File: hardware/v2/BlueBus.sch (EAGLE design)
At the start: 142 parts, among them J1 3PIN_953442_1, J2 6PIN_953442_1, J3 6PIN_5_103166_1, J4 SJ2-35853A-SMT-TR, J5 SMB_CONN, J6 USB3080-30-01-A, J7 PCM12SMTR, J8 TC2030NL, Q1 NMOSFET-BSS138K, Q2 NMOSFET-BSS138K, Q3 PMOSFET-DMP32D4SSOT323, U1 MPQ4420, U10 PCM5122, U11 PAM8406, U2 TH3122.4, U3 FT231XS, U4 S-1212BC0-U5T1U, U5 XC6210, U6 CAT25M01, U7 PIC24FJ1024GA606, U8 BM83SM1, U9 DIT4096

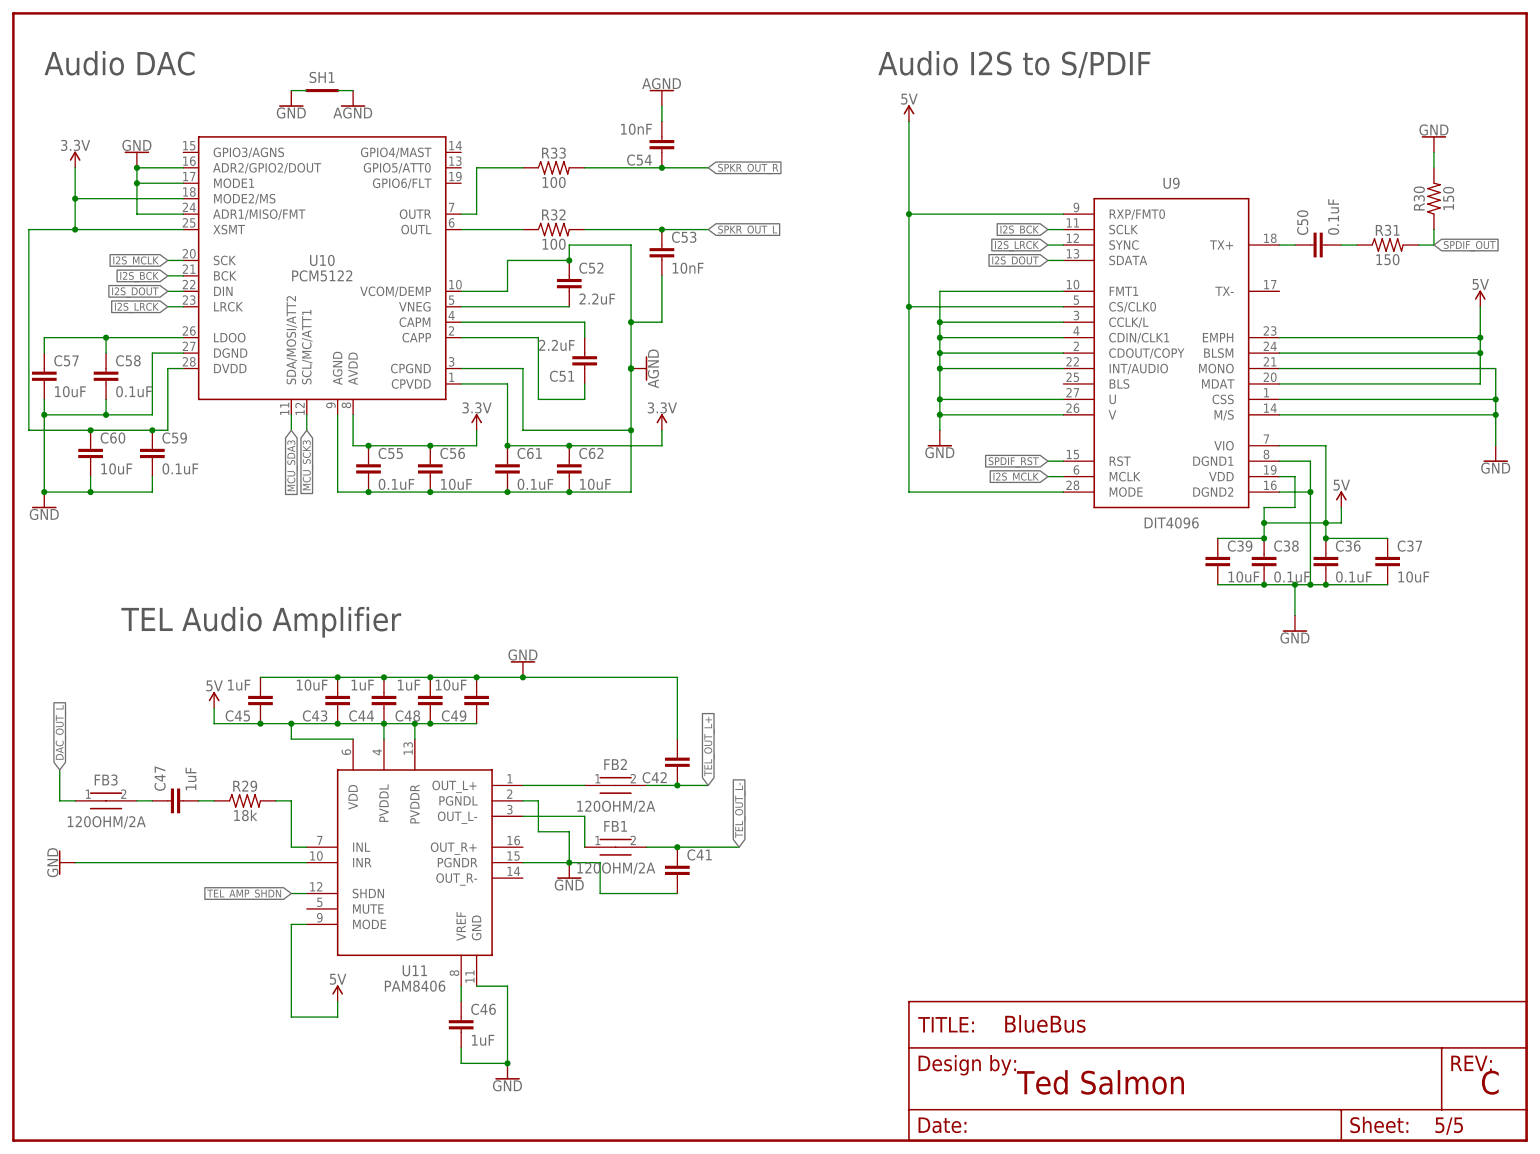
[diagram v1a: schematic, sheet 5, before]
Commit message: [IMP] hardware: v2 Bugfixes * Ensure 100nF caps are closest to pins instead of 10uF/1uF * Fix bottom silkscreen * Fix recovery slider silkscreen * Renumber passives per convention (counter-clockwise)
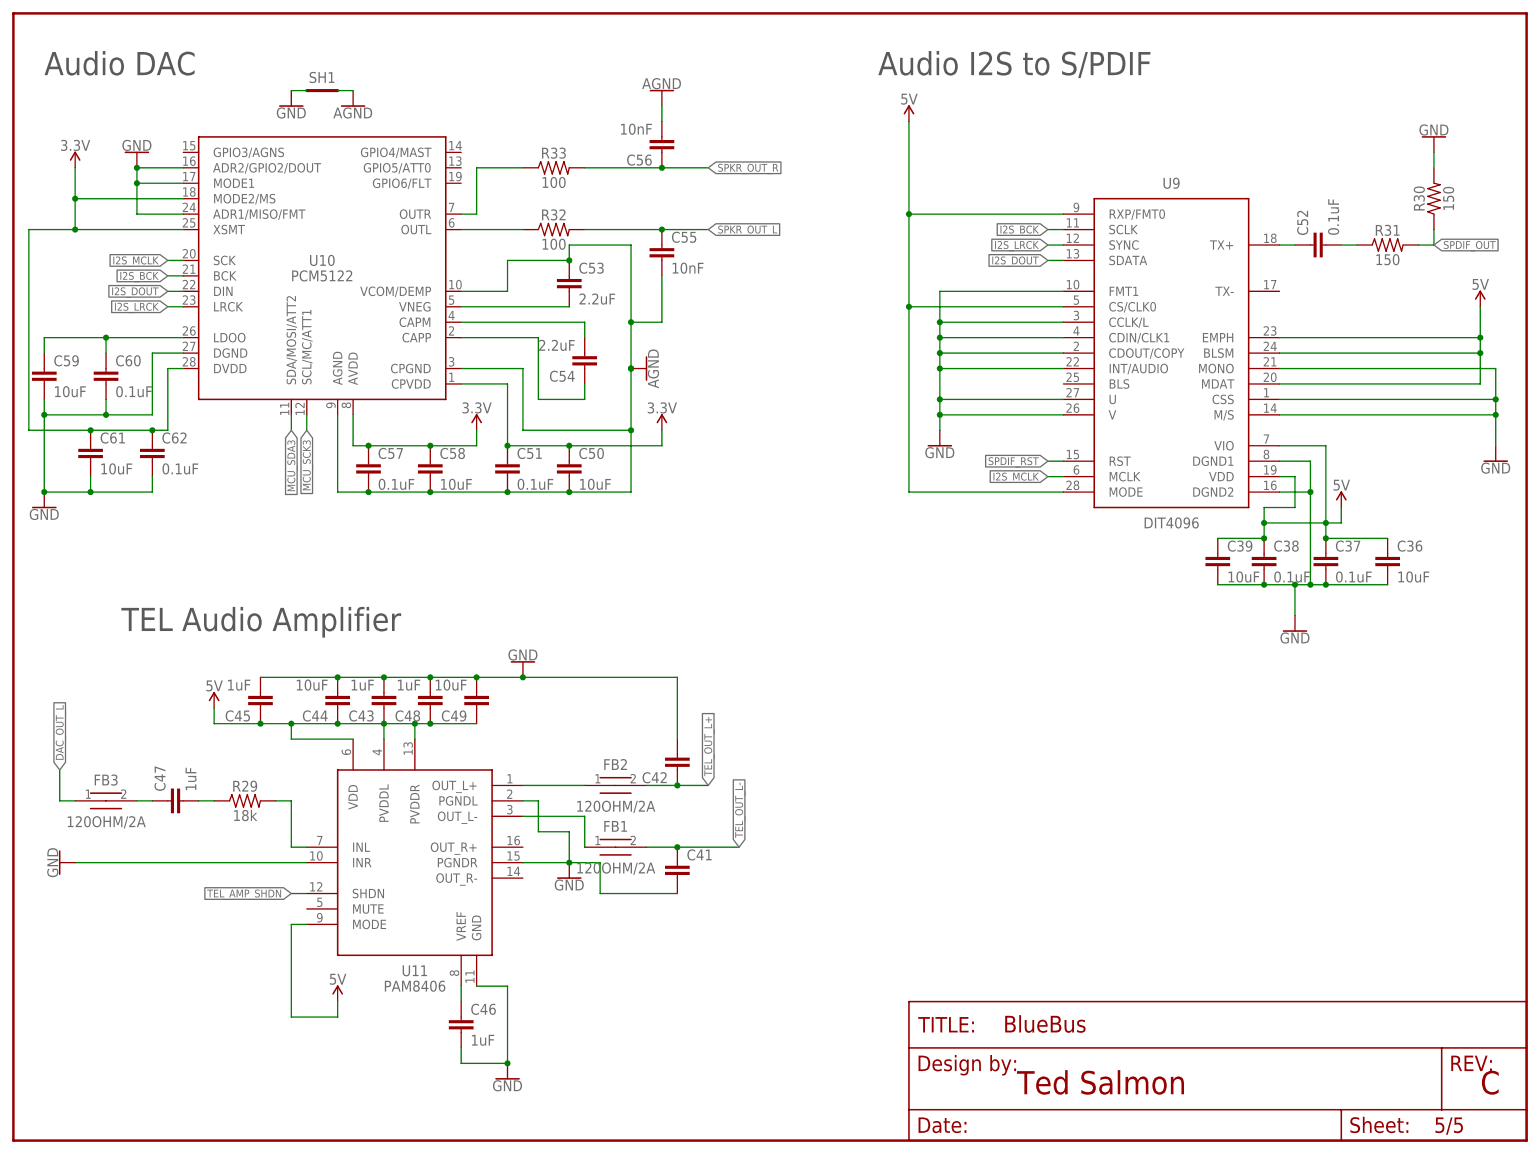
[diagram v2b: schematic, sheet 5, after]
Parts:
- C24, C36, C50, C58, C59, C61: value 0.1uF -> 10uF; device Passives:0.1UF0603 -> Passives:10UF0603
- C26, C37, C57, C60, C62: value 10uF -> 0.1uF; device Passives:10UF0603 -> Passives:0.1UF0603
- C43: value 10uF -> 1uF; device Passives:10UF0603 -> Passives:1UF0603
- C44: value 1uF -> 10uF; device Passives:1UF0603 -> Passives:10UF0603
- C51, C52: value 2.2uF -> 0.1uF; device Passives:2.2UF0603 -> Passives:0.1UF0603
- C53, C54: value 10nF -> 2.2uF; device Passives:10NF0603 -> Passives:2.2UF0603
- C55: value 0.1uF -> 10nF; device Passives:0.1UF0603 -> Passives:10NF0603
- C56: value 10uF -> 10nF; device Passives:10UF0603 -> Passives:10NF0603
- R8: value 20 -> 100k; device Passives:20OHM0603 -> Passives:100KOHM0603
- R9: value 100k -> 20; device Passives:100KOHM0603 -> Passives:20OHM0603
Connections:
- net 3.3V: now also C50.1, C51.1, C57.1, C58.1; no longer C55.1, C56.1, C59.1, C60.1
- net 5V: now also C24.1; no longer C26.1
- net 5VREG_BS: now also R9.1; no longer R8.1
- net 5VREG_BS_CAP: now also C7.1, R9.2; no longer C11.1, R8.2
- net 5VREG_EN: now also R8.1; no longer R9.1
- net 5VREG_SW: now also C7.2; no longer C11.2
- net 5VREG_VCC: now also C8.1; no longer C7.1
- net AGND: now also C50.2, C51.2, C53.1, C57.2, C58.2; no longer C52.1, C53.2, C54.2, C61.2, C62.2
- net DAC_CAPM: now also C54.2; no longer C51.2
- net DAC_CAPP: now also C54.1; no longer C51.1
- net DAC_LDOO: now also C59.1, C60.1; no longer C57.1, C58.1
- net DAC_VNEG: now also C53.2; no longer C52.2
- net GND: now also C11.2, C61.2, C62.2; no longer C57.2, C58.2, C7.2
- net IBUS_5V: now also R8.2; no longer R9.2
- net SPDIF_TX_FLT: now also C52.1; no longer C50.1
- net SPDIF_TX_RES: now also C52.2; no longer C50.2
- net SPKR_OUT_L: now also C55.1; no longer C53.1
- net SPKR_OUT_R: now also C56.1; no longer C54.1
- net USB_3V3: now also C26.1; no longer C24.1
- net VIN: now also C11.1; no longer C8.1
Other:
- moved on the sheet: C10, C11, C24, C26, C36, C37, C43, C44, C50, C51, C52, C53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

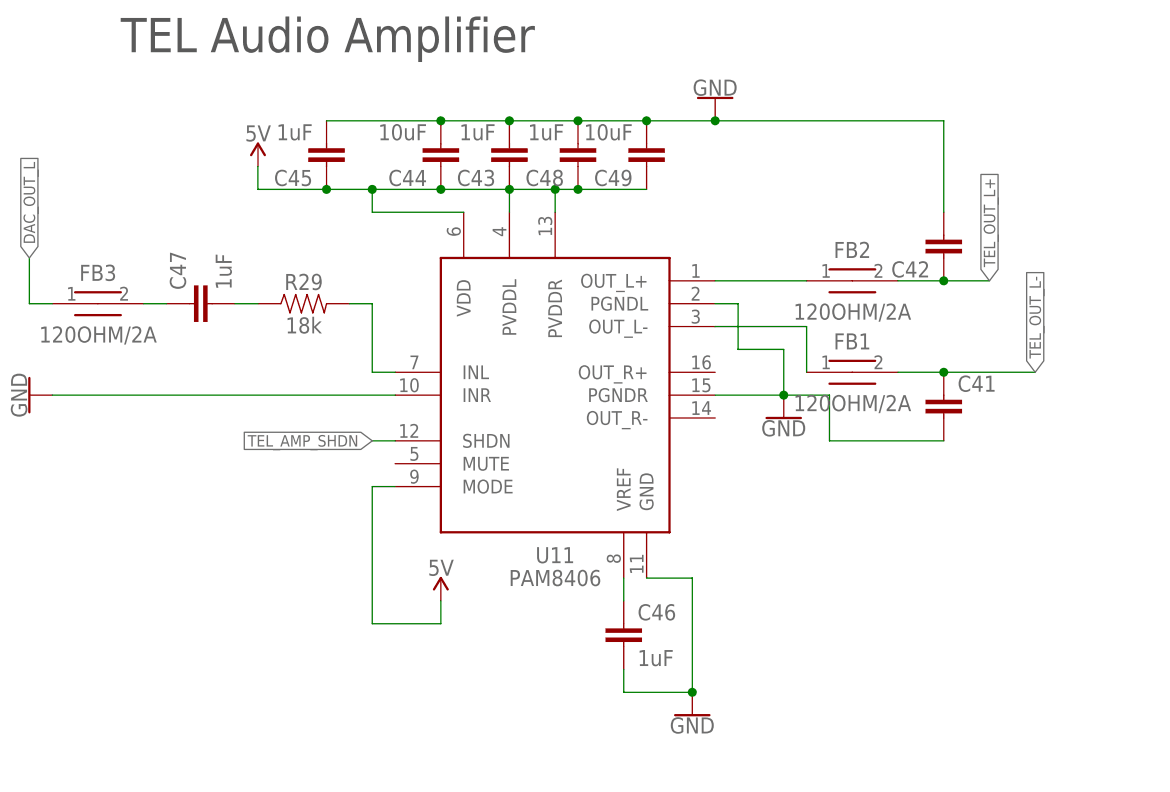
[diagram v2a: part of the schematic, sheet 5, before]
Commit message: [IMP] hardware: v2 Bugfixes * Re-number capacitors per convention and ensure proper placement
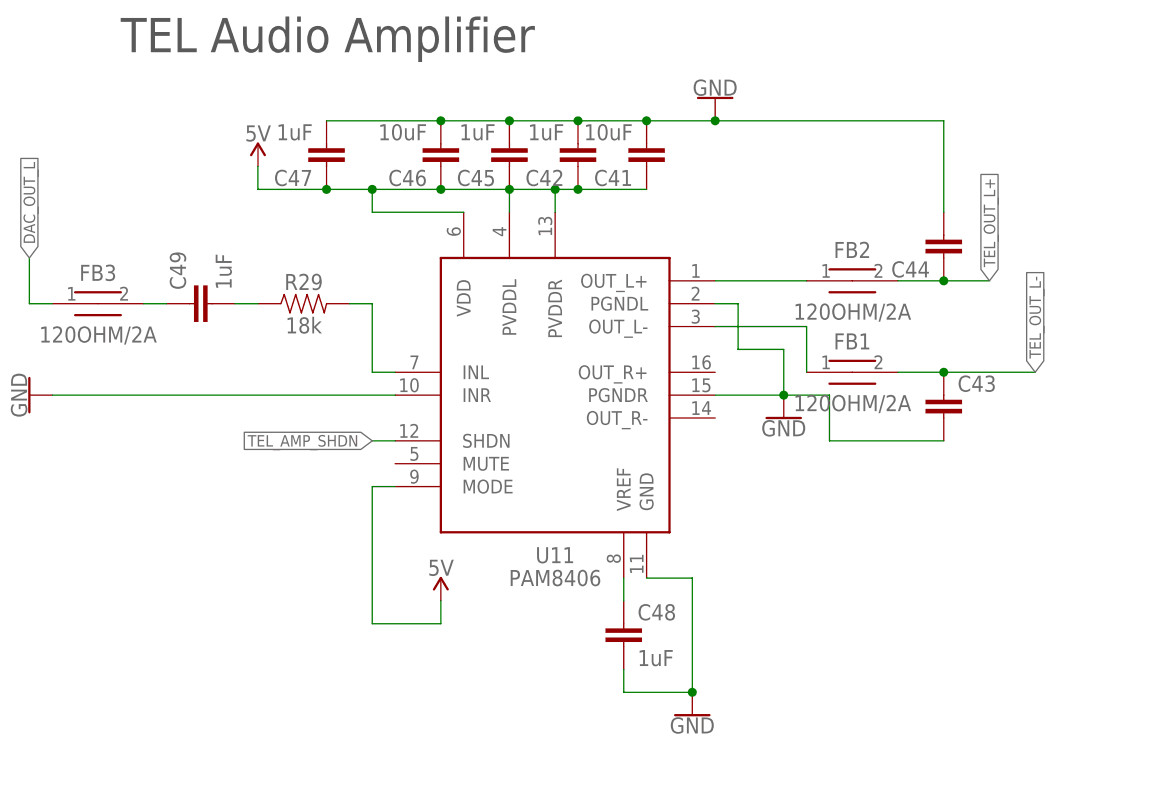
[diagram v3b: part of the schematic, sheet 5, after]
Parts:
- C1: value RHS1V101MCN1GS -> 0.1uF; device Passives:RHS1V101MCN1GS -> Passives:0.1UF0603
- C18: value 10uF -> 0.1uF; device Passives:10UF0603 -> Passives:0.1UF0603
- C19: value 0.1uF -> 10uF; device Passives:0.1UF0603 -> Passives:10UF0603
- C2: value 0.1uF -> 2.2uF; device Passives:0.1UF0603 -> Passives:2.2UF0603
- C3: value 2.2uF -> 1uF; device Passives:2.2UF0603 -> Passives:1UF0603
- C31: value 1uF -> 47nF; device Passives:1UF0603 -> Passives:47NF0603
- C32, C43: value 1uF -> 200pF; device Passives:1UF0603 -> Passives:220PF0603
- C34, C42: value 200pF -> 1uF; device Passives:220PF0603 -> Passives:1UF0603
- C35: value 47nF -> 1uF; device Passives:47NF0603 -> Passives:1UF0603
- C4: value 1uF -> RHS1V101MCN1GS; device Passives:1UF0603 -> Passives:RHS1V101MCN1GS
- C41: value 200pF -> 10uF; device Passives:220PF0603 -> Passives:10UF0603
- C44: value 10uF -> 200pF; device Passives:10UF0603 -> Passives:220PF0603
- C46: value 1uF -> 10uF; device Passives:1UF0603 -> Passives:10UF0603
- C49: value 10uF -> 1uF; device Passives:10UF0603 -> Passives:1UF0603
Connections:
- net 12V: now also C2.1; no longer C3.1
- net 3.3V: now also C1.1, C17.2; no longer C2.1, C20.2
- net 5V: now also C41.1, C42.1, C46.1, C47.1; no longer C43.1, C44.1, C48.1, C49.1
- net BT_MIC_L: now also C32.1, R27.1; no longer C34.1, R26.1
- net GND: now also C17.1, C20.2, C31.1, C35.2, C47.2; no longer C17.2, C20.1, C31.2, C35.1, C49.2
- net MCU_MCLR_RES: now also C20.1; no longer C19.1
- net MCU_VCAP: now also C19.1; no longer C17.1
- net MICN1: now also C31.2; no longer C35.2
- net MICP1_RES: now also C35.1, R26.1, R27.2; no longer C31.1, R26.2, R27.1
- net MIC_BIAS: now also C34.1, R26.2; no longer C32.1, R27.2
- net TEL_AMP_IN: now also C49.1; no longer C47.1
- net TEL_AMP_INL_CAP_RES: now also C49.2; no longer C47.2
- net TEL_AMP_VREF: now also C48.1; no longer C46.1
- net TEL_OUT_L+: now also C44.1; no longer C42.1
- net TEL_OUT_L-: now also C43.1; no longer C41.1
- net VIN: now also C3.1; no longer C1.1
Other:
- moved on the sheet: C14, C15, C16, C17, C18, C19, C2, C20, C3, C31, C32, C34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

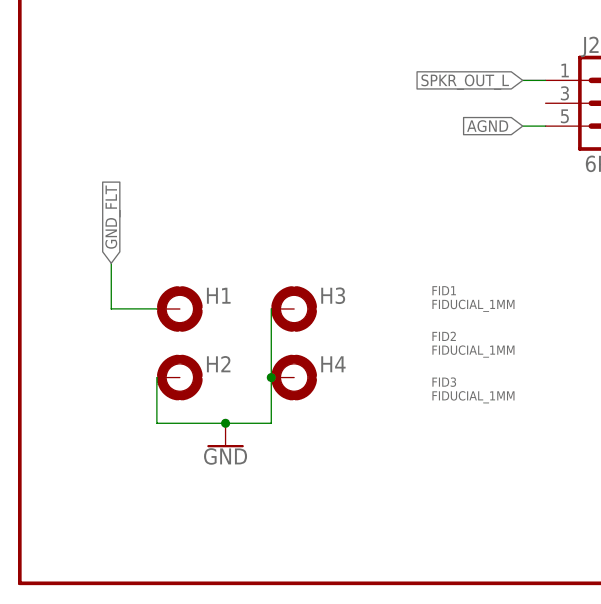
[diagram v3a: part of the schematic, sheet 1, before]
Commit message: [IMP] hardware: v2 Hardware updates for manufacture * Remove USB cutout * Swap PTH holes to simple holes * Add tCream to USB mount holes
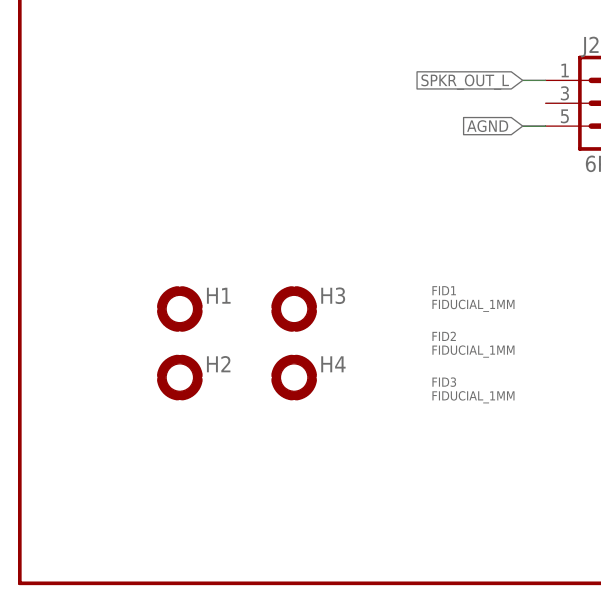
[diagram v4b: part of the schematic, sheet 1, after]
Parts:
- H1, H2, H3, H4: value 2,5-PAD -> 2,5-HOLE; device Connectors:2,5-PAD -> Connectors:2,5-HOLE
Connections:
- net GND: no longer H2.MOUNT, H3.MOUNT, H4.MOUNT
- net GND_FLT: no longer H1.MOUNT
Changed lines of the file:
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@@
 <part name="FRAME4" library="Frame" deviceset="FRAME-LETTER" device="" package3d_urn="urn:adsk.eagle:package:37104/1"/>
 <part name="U10" library="ICs" deviceset="PCM5122" device="" value="PCM5122"/>
-<part name="H1" library="Connectors" deviceset="2,5-PAD" device=""/>
-<part name="H2" library="Connectors" deviceset="2,5-PAD" device=""/>
-<part name="H3" library="Connectors" deviceset="2,5-PAD" device=""/>
-<part name="H4" library="Connectors" deviceset="2,5-PAD" device=""/>
-<part name="GND28" library="SparkFun-PowerSymbols" library_urn="urn:adsk.eagle:library:530" deviceset="GND" device=""/>
+<part name="H1" library="Connectors" deviceset="2,5-HOLE" device=""/>
+<part name="H2" library="Connectors" deviceset="2,5-HOLE" device=""/>
+<part name="H3" library="Connectors" deviceset="2,5-HOLE" device=""/>
+<part name="H4" library="Connectors" deviceset="2,5-HOLE" device=""/>
 <part name="FB3" library="Passives" deviceset="FERRITE_2A/120OHM" device="0603" value="120OHM/2A"/>
 <part name="F1" library="Passives" deviceset="LITTLEBLOCK_FUSE_.75A" device="" value="750mA"/>
@@
 <attribute name="NAME" x="33.274" y="23.4442" size="1.778" layer="95"/>
 </instance>
-<instance part="GND28" gate="1" x="22.86" y="15.24" smashed="yes">
-<attribute name="VALUE" x="22.86" y="14.986" size="1.778" layer="96" align="top-center"/>
-</instance>
 <instance part="F1" gate="G$1" x="182.88" y="157.48" smashed="yes">
 <attribute name="NAME" x="182.88" y="162.56" size="1.778" layer="95" font="vector" align="center"/>
@@
 </segment>
 <segment>
-<pinref part="H2" gate="G$1" pin="MOUNT"/>
-<pinref part="GND28" gate="1" pin="GND"/>
-<wire x1="15.24" y1="22.86" x2="15.24" y2="17.78" width="0.1524" layer="91"/>
-<wire x1="15.24" y1="17.78" x2="22.86" y2="17.78" width="0.1524" layer="91"/>
-<pinref part="H3" gate="G$1" pin="MOUNT"/>
-<pinref part="H4" gate="G$1" pin="MOUNT"/>
-<wire x1="27.94" y1="30.48" x2="27.94" y2="22.86" width="0.1524" layer="91"/>
-<wire x1="27.94" y1="22.86" x2="27.94" y2="17.78" width="0.1524" layer="91"/>
-<wire x1="27.94" y1="17.78" x2="22.86" y2="17.78" width="0.1524" layer="91"/>
-<junction x="27.94" y="22.86"/>
-<junction x="22.86" y="17.78"/>
-</segment>
-<segment>
 <pinref part="C8" gate="G$1" pin="2"/>
 <pinref part="GND31" gate="1" pin="GND"/>
@@
 </segment>
 <segment>
-<pinref part="H1" gate="G$1" pin="MOUNT"/>
-<wire x1="15.24" y1="30.48" x2="10.16" y2="30.48" width="0.1524" layer="91"/>
-<wire x1="10.16" y1="30.48" x2="10.16" y2="35.56" width="0.1524" layer="91"/>
-<label x="10.16" y="35.56" size="1.27" layer="95" rot="R90" xref="yes"/>
-</segment>
-<segment>
